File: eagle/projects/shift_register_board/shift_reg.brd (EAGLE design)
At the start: 130.8 x 80 mm, 34 parts, among them U1 SN74HC595D, U2 SN74HC595D, U3 SN74HC595D, U4 SN74HC595D

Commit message: Routed board.
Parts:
- turned R4 to 180 degrees
- turned R5 to 180 degrees
- turned R6 to 180 degrees
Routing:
- net VCC: track 245.2 -> 288.1 mm, vias 0 -> 1
- net LATCH: track 134.3 -> 172.1 mm
- net OE: track 142.7 -> 175.2 mm
- net CLOCK: track 122.0 -> 153.5 mm
- net N$15: track 0.00 -> 23.5 mm
- net N$32: track 0.00 -> 20.6 mm
- net N$31: track 0.00 -> 17.8 mm
- net N$27: track 0.00 -> 14.7 mm
- net N$30: track 0.00 -> 14.1 mm
- net N$29: track 0.00 -> 13.3 mm
- net N$6: track 199.7 -> 191.4 mm
- net Z: track 0.00 -> 8.24 mm
- net Y: track 0.00 -> 8.24 mm
- net X: track 0.00 -> 8.24 mm
- net W: track 0.00 -> 8.24 mm
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
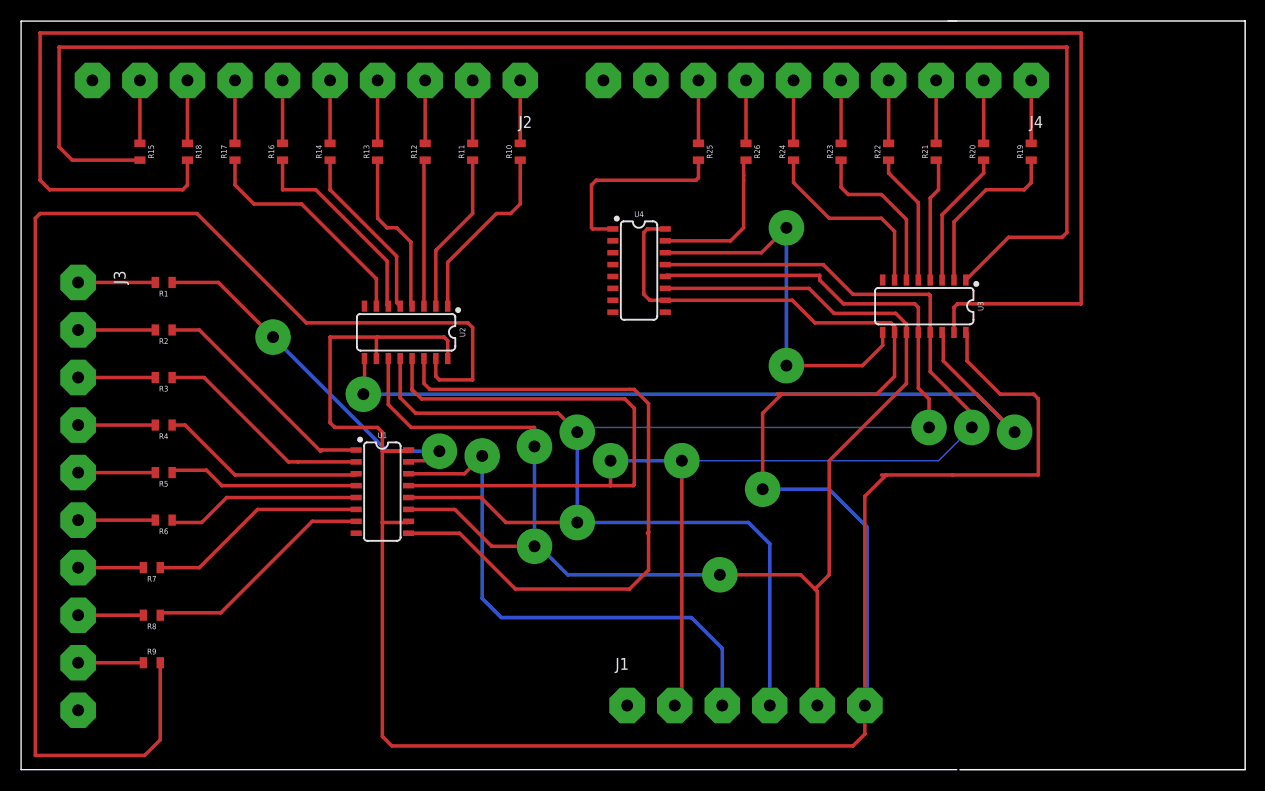
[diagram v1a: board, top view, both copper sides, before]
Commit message: Board layout using SMD components
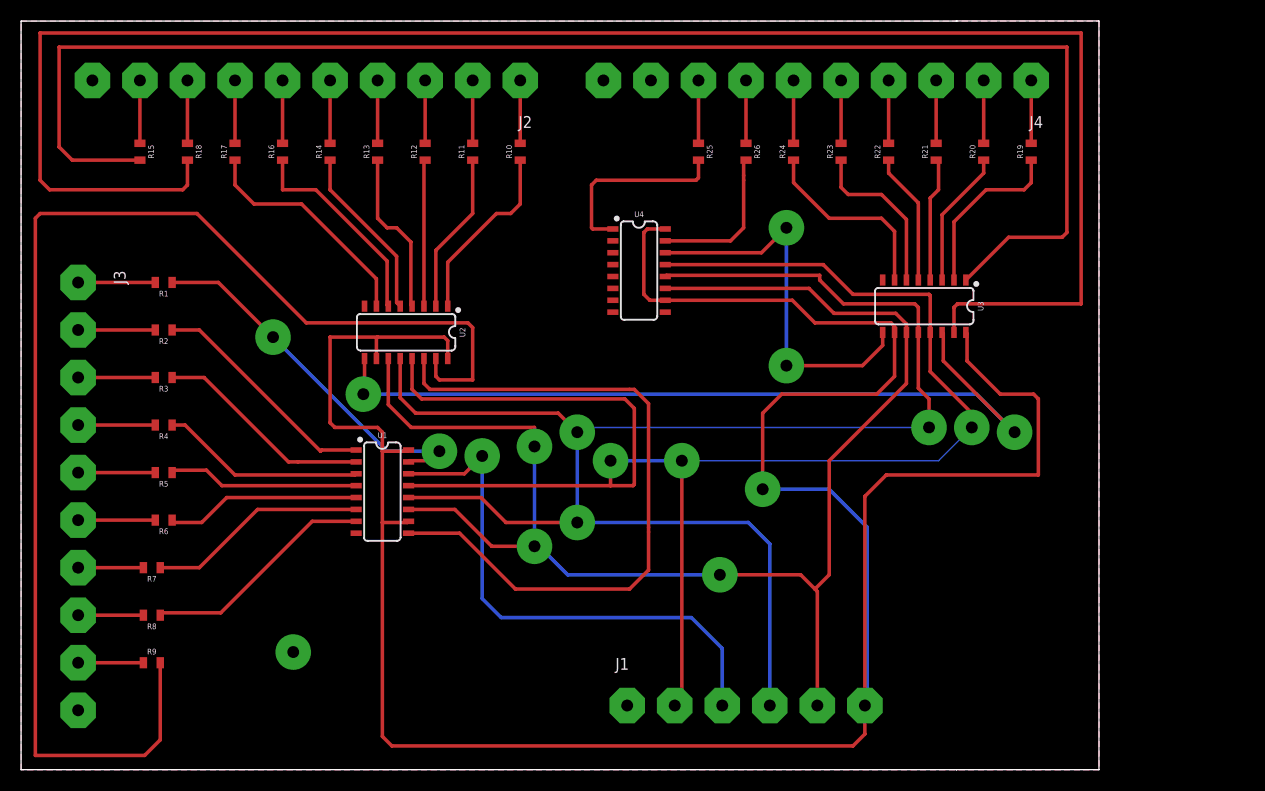
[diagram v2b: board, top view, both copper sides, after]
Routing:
- net VCC: track 288.1 -> 286.8 mm
- added copper zone on layer 1, net GND
- added copper zone on layer 16, net GND
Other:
- board size 130.8 x 80 mm -> 115.2 x 80 mm
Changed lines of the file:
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@@
 <setting verticaltext="up"/>
 </settings>
-<grid distance="20" unitdist="mil" unit="mil" style="lines" multiple="1" display="yes" altdistance="5" altunitdist="mil" altunit="mil"/>
+<grid distance="5" unitdist="mil" unit="mil" style="lines" multiple="1" display="yes" altdistance="5" altunitdist="mil" altunit="mil"/>
 <layers>
 <layer number="1" name="Top" color="4" fill="1" visible="yes" active="yes"/>
@@
 <board>
 <plain>
-<wire x1="0" y1="0" x2="100" y2="0" width="0" layer="20"/>
+<wire x1="0" y1="0" x2="99.949" y2="0" width="0" layer="20"/>
+<wire x1="99.949" y1="0" x2="100" y2="0" width="0" layer="20"/>
 <wire x1="100" y1="80" x2="0" y2="80" width="0" layer="20"/>
 <wire x1="0" y1="80" x2="0" y2="0" width="0" layer="20"/>
-<wire x1="99.06" y1="80.01" x2="130.81" y2="80.01" width="0.1524" layer="20"/>
-<wire x1="130.81" y1="80.01" x2="130.81" y2="0" width="0.1524" layer="20"/>
-<wire x1="130.81" y1="0" x2="100.33" y2="0" width="0.1524" layer="20"/>
+<wire x1="99.949" y1="80.01" x2="115.189" y2="80.01" width="0.0254" layer="20"/>
+<wire x1="115.189" y1="80.01" x2="115.189" y2="0" width="0.0254" layer="20"/>
+<wire x1="115.189" y1="0" x2="99.949" y2="0" width="0.0254" layer="20"/>
 </plain>
 <attributes>
@@
 <wire x1="38.608" y1="26.416" x2="41.281" y2="26.416" width="0.381" layer="1"/>
 <wire x1="41.281" y1="26.416" x2="41.408" y2="26.543" width="0.381" layer="1"/>
-<wire x1="92.456" y1="31.496" x2="99.568" y2="31.496" width="0.381" layer="1"/>
-<wire x1="92.456" y1="31.496" x2="91.948" y2="31.496" width="0.381" layer="1"/>
-<wire x1="93.472" y1="46.603" x2="93.345" y2="46.73" width="0.381" layer="1"/>
 <wire x1="45.593" y1="43.936" x2="45.593" y2="45.847" width="0.381" layer="1"/>
 <wire x1="45.593" y1="45.847" x2="45.212" y2="46.228" width="0.381" layer="1"/>
@@
 <wire x1="39.624" y1="2.54" x2="88.9" y2="2.54" width="0.381" layer="1"/>
 <wire x1="88.9" y1="2.54" x2="90.17" y2="3.81" width="0.381" layer="1"/>
-<wire x1="90.17" y1="3.81" x2="90.17" y2="6.858" width="0.381" layer="1"/>
 <wire x1="38.608" y1="3.556" x2="39.624" y2="2.54" width="0.381" layer="1"/>
 <wire x1="38.608" y1="34.036" x2="38.608" y2="36.068" width="0.381" layer="1"/>
@@
 <wire x1="101.092" y1="43.688" x2="104.648" y2="40.132" width="0.381" layer="1"/>
 <wire x1="108.204" y1="40.132" x2="104.648" y2="40.132" width="0.381" layer="1"/>
-<wire x1="99.568" y1="31.496" x2="108.712" y2="31.496" width="0.381" layer="1"/>
+<wire x1="92.456" y1="31.496" x2="108.712" y2="31.496" width="0.381" layer="1"/>
 <wire x1="108.712" y1="31.496" x2="108.712" y2="39.624" width="0.381" layer="1"/>
 <wire x1="108.712" y1="39.624" x2="108.204" y2="40.132" width="0.381" layer="1"/>
-<wire x1="80.772" y1="40.132" x2="81.28" y2="40.132" width="0.381" layer="1"/>
 <wire x1="81.28" y1="40.132" x2="91.44" y2="40.132" width="0.381" layer="1"/>
 <wire x1="91.44" y1="40.132" x2="93.345" y2="42.037" width="0.381" layer="1"/>
@@
 <wire x1="79.248" y1="29.972" x2="86.36" y2="29.972" width="0.381" layer="16"/>
 <wire x1="86.36" y1="29.972" x2="90.424" y2="25.908" width="0.381" layer="16"/>
-<wire x1="90.424" y1="25.908" x2="90.424" y2="6.604" width="0.381" layer="16"/>
-<wire x1="90.17" y1="6.858" x2="90.424" y2="6.604" width="0" layer="19" extent="16-16"/>
+<wire x1="90.17" y1="3.81" x2="90.17" y2="6.858" width="0.381" layer="1"/>
+<wire x1="90.424" y1="25.908" x2="90.424" y2="7.112" width="0.381" layer="16"/>
+<wire x1="90.424" y1="7.112" x2="90.17" y2="6.858" width="0.381" layer="16"/>
 </signal>
 <signal name="GND">
@@
 <contactref element="U4" pad="8"/>
 <contactref element="J4" pad="P$10"/>
-<wire x1="63.24" y1="48.895" x2="92.075" y2="52.33" width="0" layer="19" extent="1-1"/>
-<wire x1="62.23" y1="73.66" x2="63.24" y2="48.895" width="0" layer="19" extent="1-1"/>
-<wire x1="36.703" y1="49.536" x2="63.24" y2="48.895" width="0" layer="19" extent="1-1"/>
-<wire x1="35.808" y1="25.273" x2="36.703" y2="49.536" width="0" layer="19" extent="1-1"/>
-<wire x1="64.77" y1="6.858" x2="35.808" y2="25.273" width="0" layer="19" extent="1-1"/>
-<wire x1="6.096" y1="6.35" x2="35.808" y2="25.273" width="0" layer="19" extent="1-1"/>
-<wire x1="7.62" y1="73.66" x2="36.703" y2="49.536" width="0" layer="19" extent="1-1"/>
+<via x="29.083" y="12.573" extent="1-16" drill="1.27" diameter="3.81"/>
+<polygon width="0.1524" layer="1">
+<vertex x="0" y="0"/>
+<vertex x="0" y="80.01"/>
+<vertex x="115.189" y="80.01"/>
+<vertex x="115.189" y="0"/>
+</polygon>
+<polygon width="0.1524" layer="16">
+<vertex x="0" y="0"/>
+<vertex x="0" y="80.01"/>
+<vertex x="115.189" y="80.01"/>
+<vertex x="115.189" y="0"/>
+</polygon>
 </signal>
 <signal name="LATCH">
@@
 <wire x1="85.725" y1="53.975" x2="88.9" y2="50.8" width="0.381" layer="1"/>
 <wire x1="41.783" y1="43.936" x2="41.783" y2="40.64" width="0.381" layer="1"/>
-<wire x1="41.783" y1="40.64" x2="41.783" y2="40.513" width="0.381" layer="1"/>
 <wire x1="65.405" y1="30.353" x2="65.532" y2="30.48" width="0.381" layer="1"/>
 <wire x1="65.532" y1="30.48" x2="65.532" y2="38.608" width="0.381" layer="1"/>
 <wire x1="65.532" y1="38.608" x2="64.516" y2="39.624" width="0.381" layer="1"/>
-<wire x1="42.799" y1="39.624" x2="41.783" y2="40.64" width="0.381" layer="1"/>
 <wire x1="41.408" y1="30.353" x2="62.992" y2="30.353" width="0.381" layer="1"/>
 <wire x1="62.992" y1="30.353" x2="65.405" y2="30.353" width="0.381" layer="1"/>
-<wire x1="64.516" y1="39.624" x2="42.799" y2="39.624" width="0.381" layer="1"/>
+<wire x1="42.799" y1="39.624" x2="64.516" y2="39.624" width="0.381" layer="1"/>
 <wire x1="62.992" y1="30.353" x2="62.992" y2="33.02" width="0.381" layer="1"/>
 <via x="62.992" y="33.02" extent="1-16" drill="1.27" diameter="3.81"/>
@@
 <wire x1="101.6" y1="36.576" x2="98.044" y2="33.02" width="0.1524" layer="16"/>
 <wire x1="98.044" y1="33.02" x2="70.612" y2="33.02" width="0.1524" layer="16"/>
+<wire x1="41.783" y1="40.64" x2="42.799" y2="39.624" width="0.381" layer="1"/>
 </signal>
 <signal name="Z">
@@
 <contactref element="U1" pad="9"/>
 <contactref element="U2" pad="14"/>
-<wire x1="66.929" y1="25.273" x2="67.056" y2="25.4" width="0.381" layer="1"/>
 <wire x1="67.056" y1="25.4" x2="67.056" y2="25.908" width="0.381" layer="1"/>
 <wire x1="67.056" y1="25.908" x2="67.056" y2="39.116" width="0.381" layer="1"/>
@@
 <contactref element="R9" pad="2"/>
 <contactref element="U2" pad="15"/>
-<wire x1="44.323" y1="43.936" x2="44.196" y2="44.063" width="0.381" layer="1"/>
 <wire x1="30.48" y1="47.752" x2="18.796" y2="59.436" width="0.381" layer="1"/>
 <wire x1="18.796" y1="59.436" x2="2.032" y2="59.436" width="0.381" layer="1"/>

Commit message: Laid out board with through holes. Ready for pour
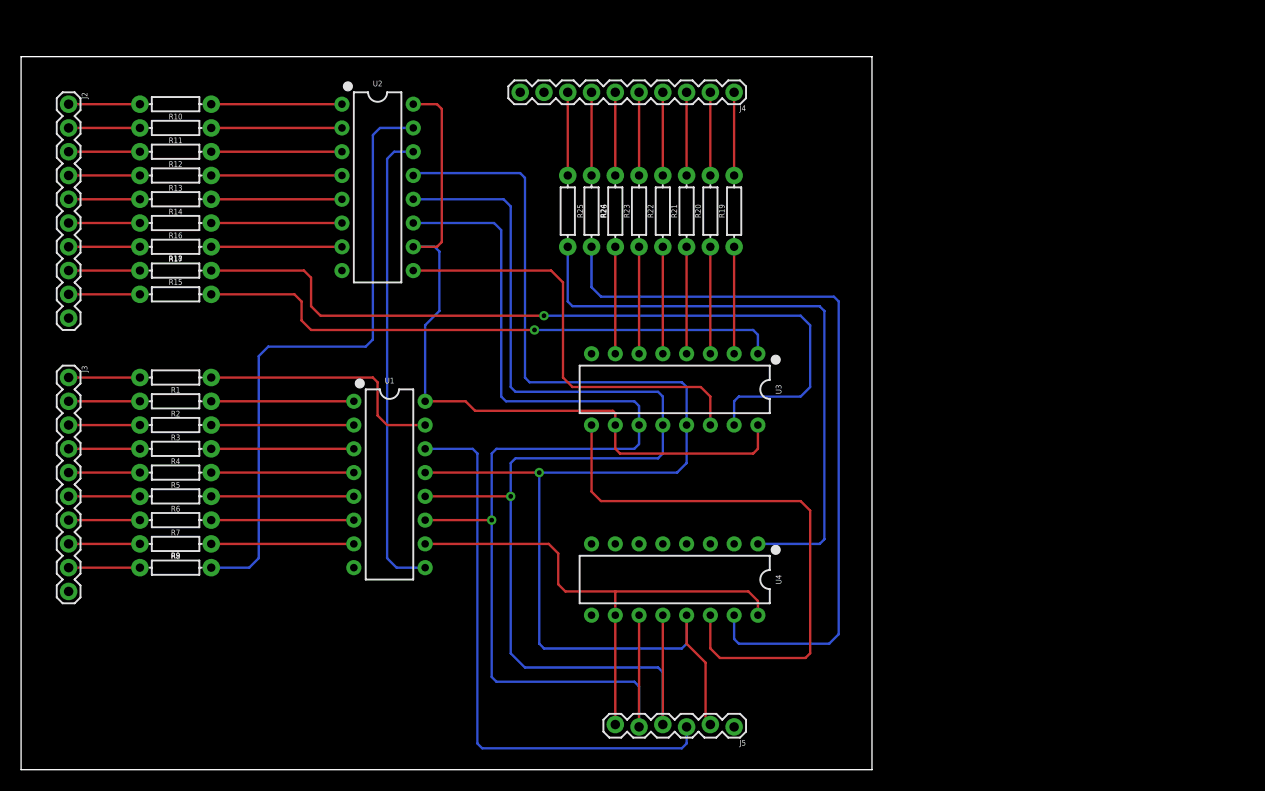
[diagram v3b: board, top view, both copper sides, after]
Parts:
- removed J1: (no value), shift_register:1X06_WIDE
- added J5: (no value), SparkFun-Connectors:1X06_LOCK
- J2, J3, J4: device shift_register:WIDE -> shift_register:1X10
- R1, R10, R11, R12, R13, R14, R15, R16, R17, R18, R19, R2, R20, R21, R22, R23, R24, R25, R26, R3, R4, R5, R6, R7, R8, R9: device SparkFun-Resistors:0805 -> SparkFun-Resistors:AXIAL-0.3
- U1, U2, U3, U4: value SN74HC595D -> SN74HC595N; device SparkFun-IC-Logic:SO16 -> SparkFun-IC-Logic:DIP16
- moved J2 48.3 mm to (5.08, 71.1), turned to 270 degrees
- moved R10 37.2 mm to (16.5, 71.1), turned to 180 degrees
- moved U4 33.2 mm to (69.8, 20.3), turned to 180 degrees
- moved R19 32.4 mm to (76.2, 59.7)
- moved R11 31.9 mm to (16.5, 68.6), turned to 180 degrees
- moved J4 31.8 mm to (76.2, 72.4)
- moved R20 29.9 mm to (73.7, 59.7)
- moved U3 28.1 mm to (69.8, 40.6)
- moved R21 27.4 mm to (71.1, 59.7)
- moved R12 26.7 mm to (16.5, 66.0), turned to 180 degrees
- moved R22 25.0 mm to (68.6, 59.7)
- moved R23 22.5 mm to (66.0, 59.7)
- moved R13 21.7 mm to (16.5, 63.5), turned to 180 degrees
- moved R24 20.1 mm to (63.5, 59.7)
- moved R26 17.7 mm to (61.0, 59.7)
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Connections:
- net A: now also J4.8, R25.P$1; no longer J4.P$8, R25.1
- net B: now also J4.7, R26.P$1; no longer J4.P$7, R26.1
- net C: now also J4.6, R24.P$2; no longer J4.P$6, R24.2
- net CLOCK: now also J5.5; no longer J1.P$5
- net D: now also J4.5, R23.P$2; no longer J4.P$5, R23.2
- net DATA: now also J5.3; no longer J1.P$3
- net E: now also J4.4, R22.P$2; no longer J4.P$4, R22.2
- net F: now also J4.3, R21.P$2; no longer J4.P$3, R21.2
- net G: now also J4.2, R20.P$2; no longer J4.P$2, R20.2
- net GND: now also J2.10, J3.10, J4.10, J5.1; no longer J1.P$1, J2.P$10, J3.P$10, J4.P$10
- net H: now also J4.1, R19.P$2; no longer J4.P$1, R19.2
- net I: now also J2.9, R15.P$1; no longer J2.P$9, R15.1
- net J: now also J2.8, R18.P$1; no longer J2.P$8, R18.1
- net K: now also J2.7, R17.P$2; no longer J2.P$7, R17.2
- net L: now also J2.6, R16.P$2; no longer J2.P$6, R16.2
- net LATCH: now also J5.4; no longer J1.P$4
- net M: now also J2.5, R14.P$2; no longer J2.P$5, R14.2
- net N: now also J2.4, R13.P$2; no longer J2.P$4, R13.2
- net N$10: now also R2.P$1; no longer R2.1
- net N$11: now also R3.P$1; no longer R3.1
- net N$12: now also R4.P$1; no longer R4.1
- net N$13: now also R5.P$1; no longer R5.1
- net N$14: now also R6.P$1; no longer R6.1
- net N$15: now also R7.P$1; no longer R7.1
- net N$16: now also R8.P$1; no longer R8.1
- net N$19: now also R10.P$1; no longer R10.1
- net N$20: now also R11.P$1; no longer R11.1
- net N$21: now also R12.P$1; no longer R12.1
- net N$22: now also R13.P$1; no longer R13.1
- net N$23: now also R16.P$1; no longer R16.1
- net N$24: now also R17.P$1; no longer R17.1
- net N$26: now also R19.P$1; no longer R19.1
- net N$27: now also R20.P$1; no longer R20.1
- net N$29: now also R21.P$1; no longer R21.1
- net N$3: now also R9.P$2; no longer R9.2
- net N$30: now also R22.P$1; no longer R22.1
- net N$31: now also R23.P$1; no longer R23.1
- net N$32: now also R24.P$1; no longer R24.1
- net N$35: now also R26.P$2; no longer R26.2
- net N$36: now also R25.P$2; no longer R25.2
- net N$4: now also R14.P$1; no longer R14.1
- net N$6: now also R18.P$2; no longer R18.2
- net N$7: now also R15.P$2; no longer R15.2
- net N$9: now also R1.P$1; no longer R1.1
- net O: now also J2.3, R12.P$2; no longer J2.P$3, R12.2
- net OE: now also J5.2; no longer J1.P$2
- net P: now also J2.2, R11.P$2; no longer J2.P$2, R11.2
- net Q: now also J2.1, R10.P$2; no longer J2.P$1, R10.2
- net R: now also J3.9, R9.P$1; no longer J3.P$9, R9.1
- net S: now also J3.8, R8.P$2; no longer J3.P$8, R8.2
- net T: now also J3.7, R7.P$2; no longer J3.P$7, R7.2
- net U: now also J3.6, R6.P$2; no longer J3.P$6, R6.2
- net V: now also J3.5, R5.P$2; no longer J3.P$5, R5.2
- net VCC: now also J5.6; no longer J1.P$6
- net W: now also J3.4, R4.P$2; no longer J3.P$4, R4.2
- net X: now also J3.3, R3.P$2; no longer J3.P$3, R3.2
- net Y: now also J3.2, R2.P$2; no longer J3.P$2, R2.2
- net Z: now also J3.1, R1.P$2; no longer J3.P$1, R1.2
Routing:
- net VCC: track 286.8 -> 139.0 mm, vias 1 -> 0
- net N$6: track 191.4 -> 86.1 mm, vias 0 -> 1
- net N$7: track 160.3 -> 63.4 mm, vias 0 -> 1
- net N$3: track 143.3 -> 66.5 mm
- net N$35: track 16.3 -> 81.3 mm
- net N$36: track 20.5 -> 65.4 mm
- net N$28: track 89.0 -> 46.3 mm, vias 2 -> 0
- net LATCH: track 172.1 -> 133.3 mm, vias 3 -> 1
- net OE: track 175.0 -> 138.0 mm, vias 3 -> 1
- net CLOCK: track 153.5 -> 126.3 mm, vias 3 -> 1
- net N$2: track 74.3 -> 50.3 mm
- net N$37: track 41.4 -> 61.4 mm, vias 2 -> 0
- net N$9: track 39.8 -> 27.0 mm, vias 2 -> 0
- net N$24: track 24.8 -> 14.0 mm
- net N$16: track 25.1 -> 15.2 mm
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- removed copper zone on layer 1, net GND
- removed copper zone on layer 16, net GND
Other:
- board size 115.2 x 80 mm -> 90.9 x 76.2 mm

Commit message: Looks like PCB Way will work. Ready to finalize design for manufacture
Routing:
- net VCC: track 139.0 -> 166.6 mm, vias 0 -> 1
- added copper zone on layer 1, net GND
